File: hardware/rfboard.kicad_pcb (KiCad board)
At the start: 2 copper layers, 23.4 x 35 mm, 24 parts, among them J1 10118194-0001LF, J2 Conn_01x10, J3 Conn_01x10, P2 CONN_01X03, P3 CONN_01X04, U1 SAMD21E18, U2 RFM69CW-915MHZ, U3 MIC5504-3.3YM5-T5, U4 74LVC1G125

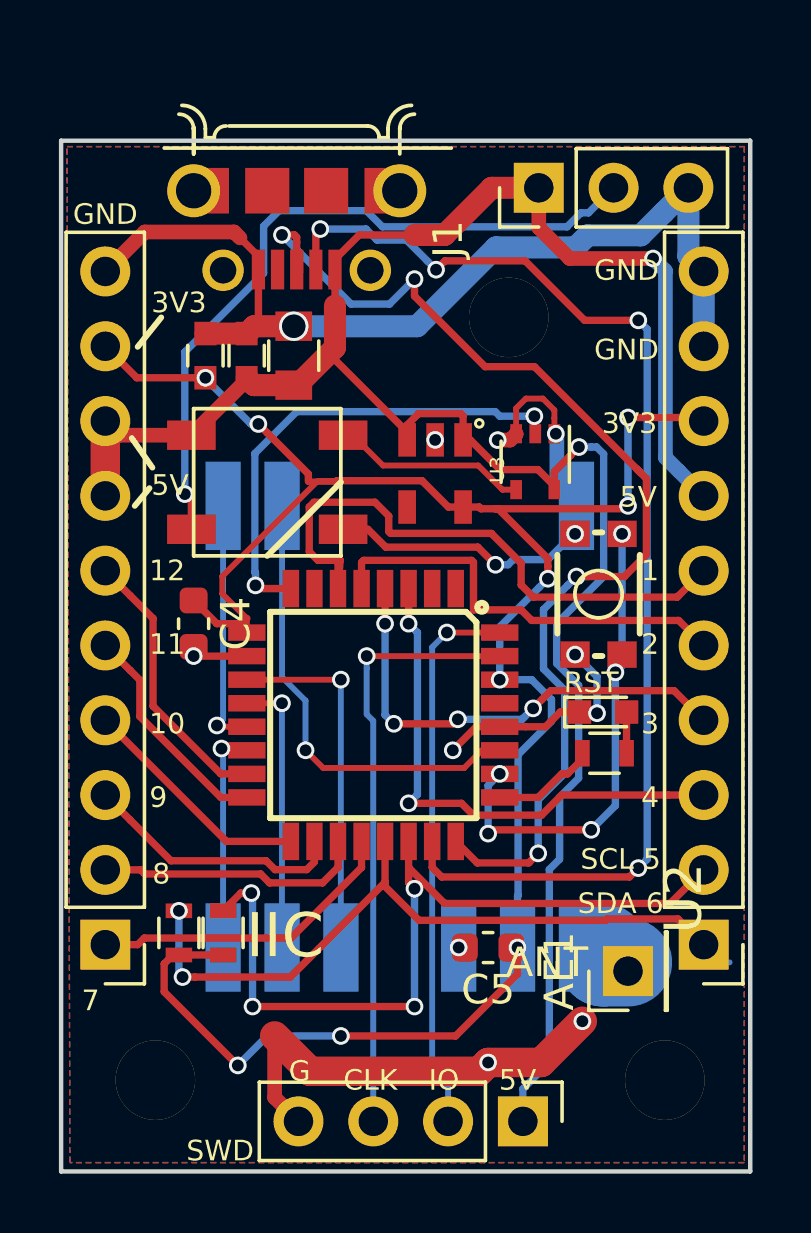
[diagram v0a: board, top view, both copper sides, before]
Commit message: Hardware revision v1.4:
- Add solder mask dam between pads on processor, regulator, buffer, and USB port
- Move antenna to not interfere with RFM69
- Added strain relief holes for LED connector
- Move USB capacitors down slightly to aid in fixing USB port shorts
- Fixed labeling of 3v3 pin
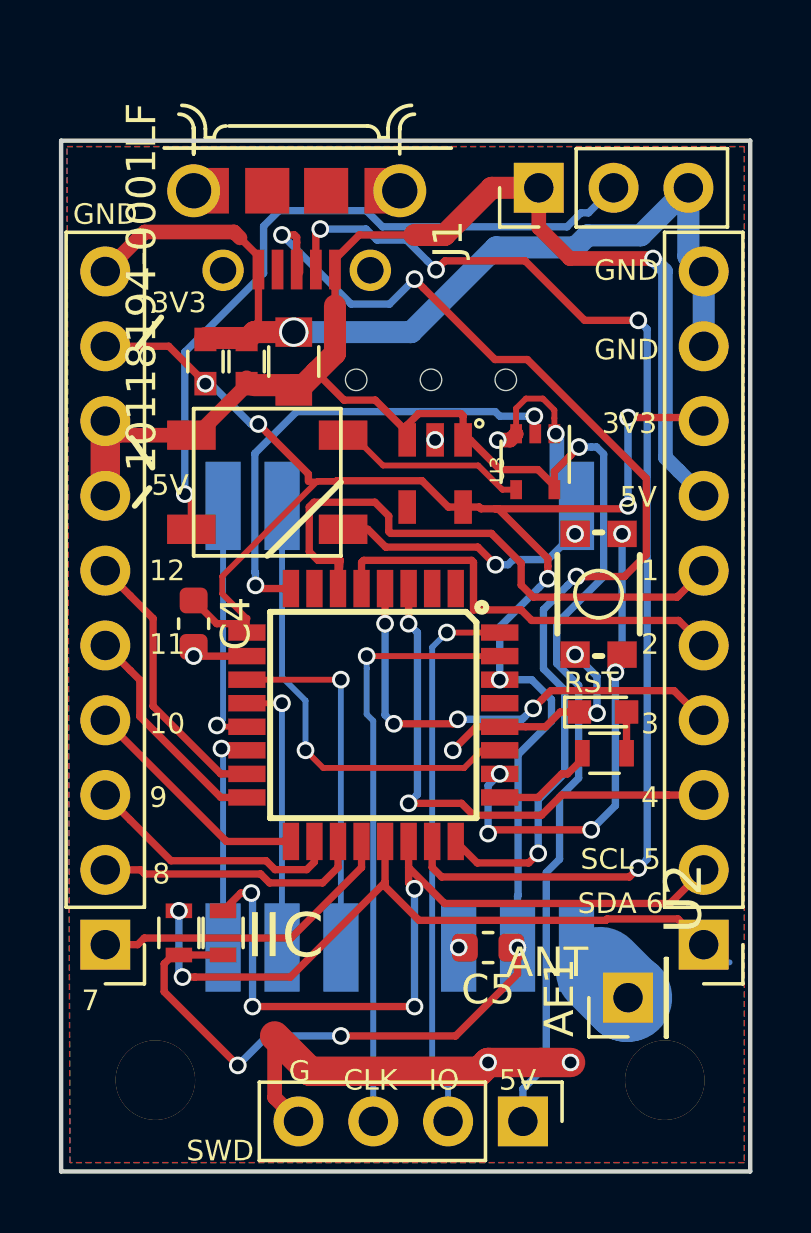
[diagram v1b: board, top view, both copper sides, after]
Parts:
- H3: value HOLE -> STRAIN_RELIEF; footprint homebrew:MountingHole_2.7mm_M2.5 -> homebrew:3_pin_2.54mm_pitch_strain_relief
- J1: footprint 10118194-0001LF:FRAMATOME_10118194-0001LF -> homebrew:FRAMATOME_10118194-0001LF_fixed_bridges
- moved H3 3.39 mm to (118.6, 135.7)
- moved AE1 0.90 mm to (125.2, 156.7)
- moved C1 0.20 mm to (110.9, 135.1)
- moved C2 0.20 mm to (112.3, 135.1)
- moved C3 0.20 mm to (113.9, 135.1)
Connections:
- J1 pad 4: Net-(J1-Pad4) -> (no net)
- U1 pad 1: Net-(U1-Pad1) -> (no net)
- U1 pad 2: Net-(U1-Pad2) -> (no net)
- U1 pad 29: Net-(U1-Pad29) -> (no net)
- U1 pad 7: Net-(U1-Pad7) -> (no net)
- U2 pad 10: Net-(U2-Pad10) -> (no net)
- U2 pad 11: Net-(U2-Pad11) -> (no net)
- U2 pad 12: Net-(U2-Pad12) -> (no net)
- U2 pad 13: Net-(U2-Pad13) -> (no net)
- U2 pad 4: Net-(U2-Pad4) -> (no net)
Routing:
- net GND: track 73.3 -> 72.4 mm
- net ANTENNA: track 2.20 -> 1.32 mm
- net USB_D+: track 38.6 -> 38.1 mm
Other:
- board text added: "3v3"
- board text added: "rfboard v1.4"
- board text removed: "rfboard v1.3"

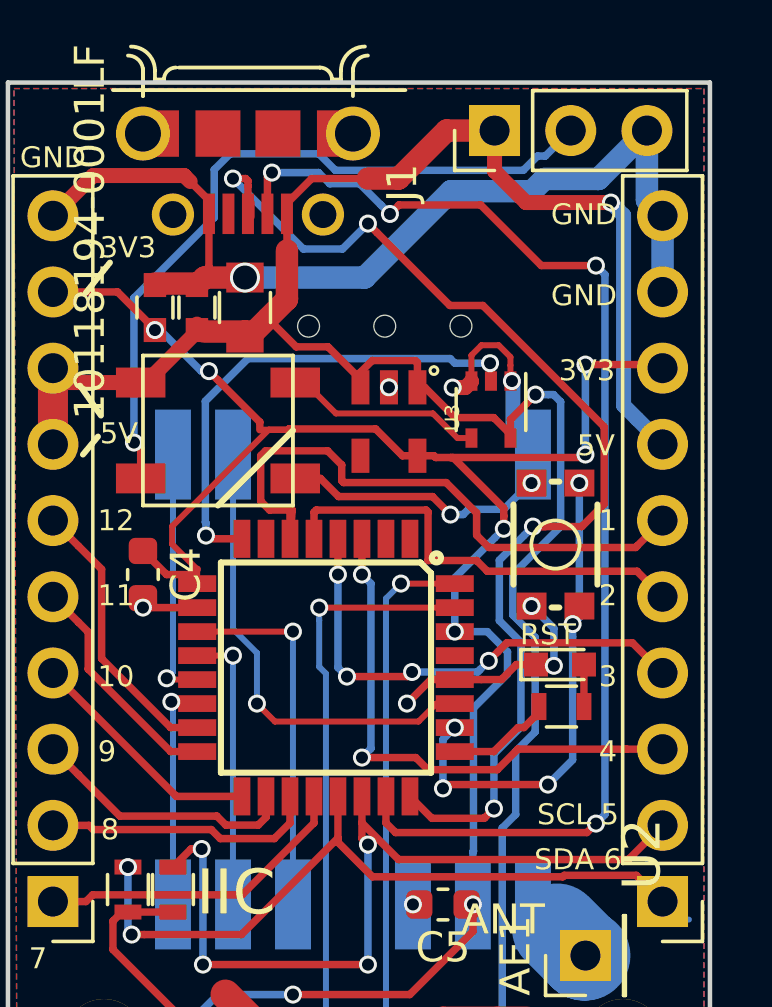
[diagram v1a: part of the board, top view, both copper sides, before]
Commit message: Revision v1.5:
- Fix size of strain relief holes
- Reduce size of stencil holes for USB port
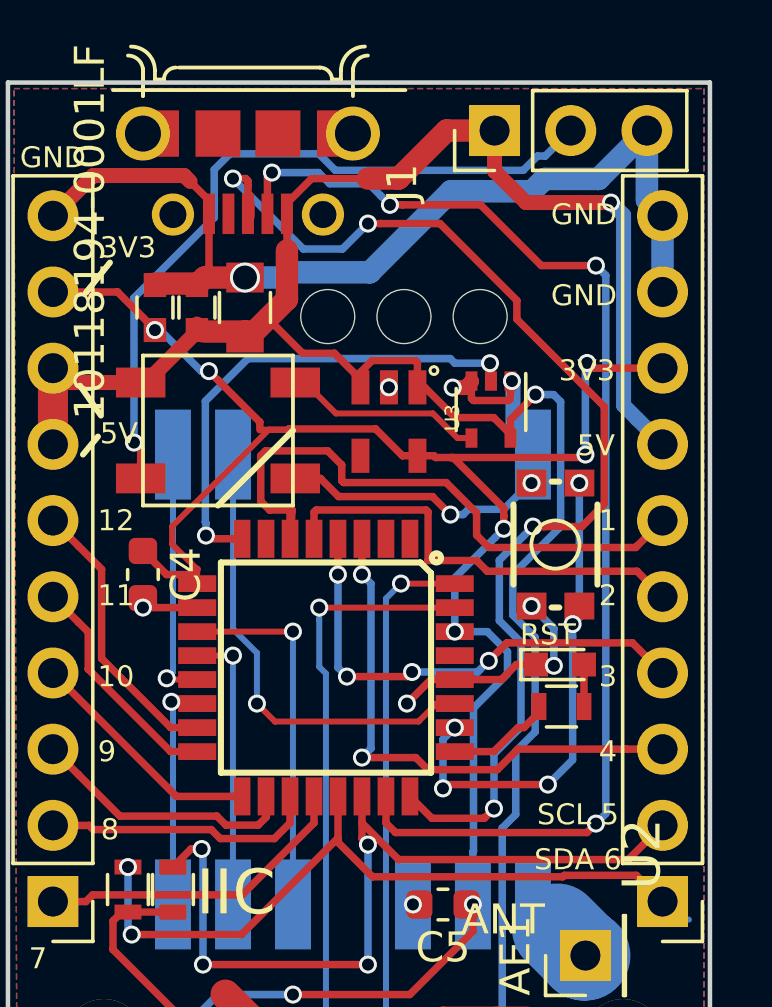
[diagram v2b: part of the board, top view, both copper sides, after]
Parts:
- moved H3 0.72 mm to (119.2, 135.4)
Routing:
- net USB_D+: track 38.1 -> 38.8 mm
- net GND: track 72.4 -> 71.6 mm
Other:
- board text added: "rfboard v1.5"
- board text removed: "TEST"
- board text removed: "rfboard v1.4"

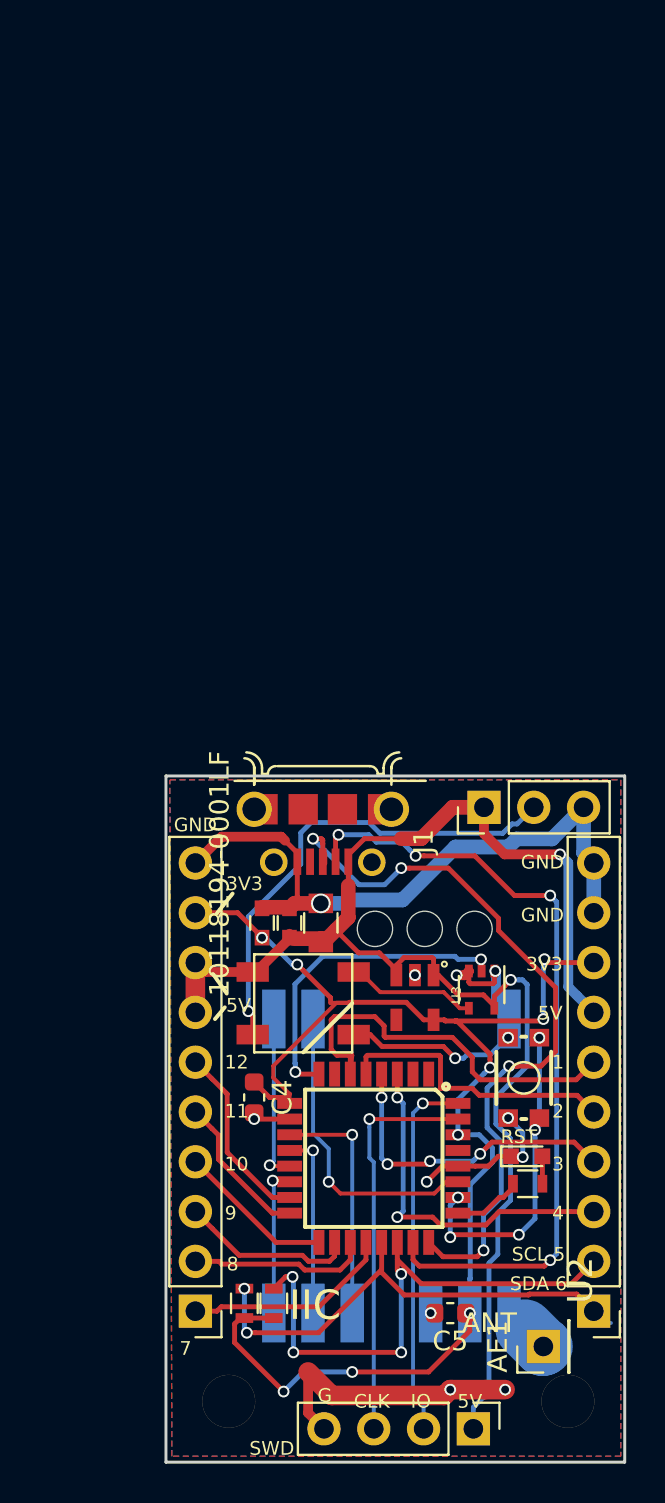
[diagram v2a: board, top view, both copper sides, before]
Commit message: Revision 1.6:
- Add PCB trace antenna, based on: http://www.ti.com/lit/an/swra416/swra416.pdf
- Change form factor to be slightly narrower
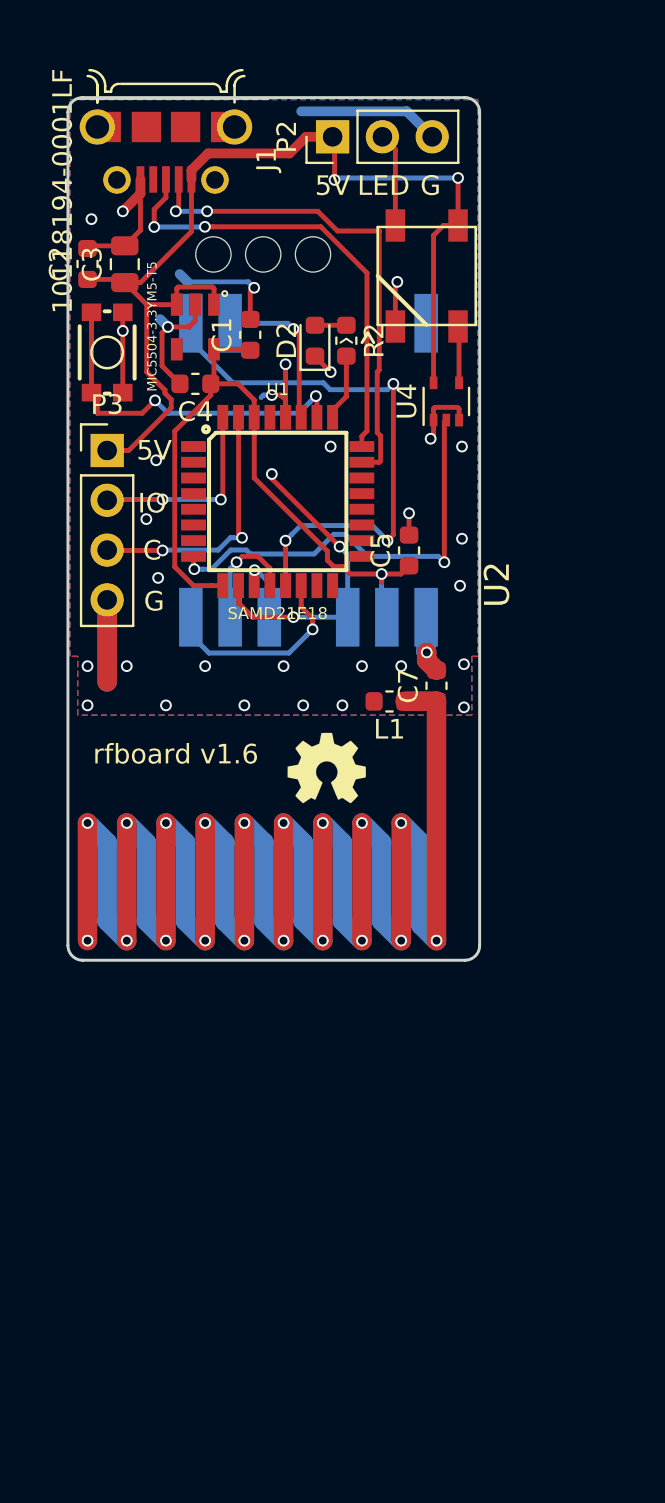
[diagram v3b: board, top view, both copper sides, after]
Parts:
- removed AE1: Antenna, Connector_PinHeader_2.54mm:PinHeader_1x01_P2.54mm_Vertical
- removed H1, H2: HOLE, homebrew:MountingHole_2.7mm_M2.5
- removed J2, J3: Conn_01x10, Pin_Headers:Pin_Header_Straight_1x10_Pitch2.54mm
- removed R1, R3: 4k7, Resistors_SMD:R_0603
- added C7: 1pF, Capacitor_SMD:C_0603_1608Metric, F.Cu at (119.8, 123.0)
- added G***: OSHW_LOGO_4mm, homebrew:OSHW_LOGO_4mm, F.Cu at (114.2, 127.2)
- added L1: 10nH, Inductor_SMD:L_0603_1608Metric, F.Cu at (117.4, 123.8)
- C1, C2: footprint Capacitors_SMD:C_0603 -> Capacitor_SMD:C_0603_1608Metric
- C3: footprint Capacitors_SMD:C_0805 -> Capacitor_SMD:C_0805_2012Metric
- D2: footprint LEDs:LED_0603 -> LED_SMD:LED_0603_1608Metric
- P2: footprint Pin_Headers:Pin_Header_Straight_1x03_Pitch2.54mm -> Connector_PinHeader_2.54mm:PinHeader_1x03_P2.54mm_Vertical
- P3: footprint Pin_Headers:Pin_Header_Straight_1x04_Pitch2.54mm -> Connector_PinHeader_2.54mm:PinHeader_1x04_P2.54mm_Vertical
- R2: footprint Resistors_SMD:R_0603 -> Resistor_SMD:R_0603_1608Metric
- S1: footprint SparkFun-Switches:TACTILE_SWITCH_SMD_4.6X2.8MM -> Sparkfun-Switches:TACTILE_SWITCH_SMD_4.6X2.8MM
- U4: footprint TO_SOT_Packages_SMD:SOT-353_SC-70-5 -> Package_TO_SOT_SMD:SOT-353_SC-70-5
- moved P3 53.3 mm to (103.0, 111.0), turned to 0 degrees
- moved R2 44.0 mm to (115.2, 105.4), turned to 270 degrees
- moved D2 43.0 mm to (113.6, 105.4), turned to 90 degrees
- moved S1 42.7 mm to (103.0, 106.0), turned to 90 degrees
- moved C5 39.0 mm to (118.4, 116.1), turned to 90 degrees
- moved D1 37.6 mm to (119.3, 102.1), turned to 270 degrees
- moved C4 36.5 mm to (107.5, 107.6), turned to 180 degrees
- moved U3 36.0 mm to (107.5, 104.7)
- moved U2 35.7 mm to (113.3, 112.0)
- moved J1 35.7 mm to (106.0, 94.5)
- moved H3 35.4 mm to (111.0, 101.0)
- moved C2 35.2 mm to (102.0, 101.5)
- moved P2 35.1 mm to (114.5, 95.0)
- moved C3 35.1 mm to (103.9, 101.5)
- moved U1 33.9 mm to (111.7, 113.6), turned to 0 degrees
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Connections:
- U1 pad 15: L6 -> (no net)
- U1 pad 16: L5 -> (no net)
- U1 pad 17: L4 -> (no net)
- U1 pad 18: L3 -> (no net)
- U1 pad 19: L2 -> (no net)
- U1 pad 20: L1 -> (no net)
- U1 pad 21: SDA -> (no net)
- U1 pad 22: SCL -> (no net)
- U1 pad 3: R3 -> (no net)
- U1 pad 4: R4 -> (no net)
- U1 pad 5: R5 -> (no net)
- U1 pad 6: R6 -> (no net)
- U2 pad 1: ANTENNA -> Net-(C6-Pad2)
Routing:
- net ANTENNA: track 1.32 -> 129.2 mm, vias 0 -> 19
- net +3V3: track 73.7 -> 36.3 mm, vias 9 -> 1
- net SCL: track 28.0 -> 0.00 mm, vias 4 -> 0
- net SDA: track 23.9 -> 0.00 mm, vias 2 -> 0
- net +5V: track 76.7 -> 54.1 mm
- net R6: track 20.5 -> 0.00 mm
- net RADIO_MISO: track 8.58 -> 28.6 mm, vias 1 -> 3
- net LED_EXTERNAL: track 24.4 -> 4.80 mm, vias 1 -> 0
- net R3: track 18.0 -> 0.00 mm, vias 2 -> 0
- net R4: track 16.1 -> 0.00 mm, vias 4 -> 0
- net USB_D+: track 38.8 -> 23.5 mm, vias 4 -> 2
- net USB_D-: track 40.5 -> 25.3 mm, vias 4 -> 2
- net R5: track 14.7 -> 0.00 mm
- net L1: track 10.7 -> 0.00 mm
- net L6: track 9.41 -> 0.00 mm
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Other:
- board size 23.4 x 35 mm -> 21 x 44 mm
- board text added: "C"
- board text added: "I"
- board text added: "rfboard v1.6"
- board text removed: "1"
- board text removed: "10"
- board text removed: "11"
- board text removed: "12"
- board text removed: "2"
- board text removed: "2812"
- board text removed: "3"
- board text removed: "3V3"
- board text removed: "3v3"
- board text removed: "4"
- board text removed: "7"
- board text removed: "8"
- board text removed: "9"
- board text removed: "ANT"
- board text removed: "BUF"
- board text removed: "CLK"
- board text removed: "IIC"
- board text removed: "RST"
- board text removed: "SCL 5"
- board text removed: "SDA 6"
- board text removed: "SW"
- board text removed: "SWD"
- board text removed: "rfboard v1.5"
